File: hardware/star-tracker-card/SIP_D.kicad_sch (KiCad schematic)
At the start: 22 parts, among them J3 CONN_03LONGPADS, U7 OSD3358-512M-BSM

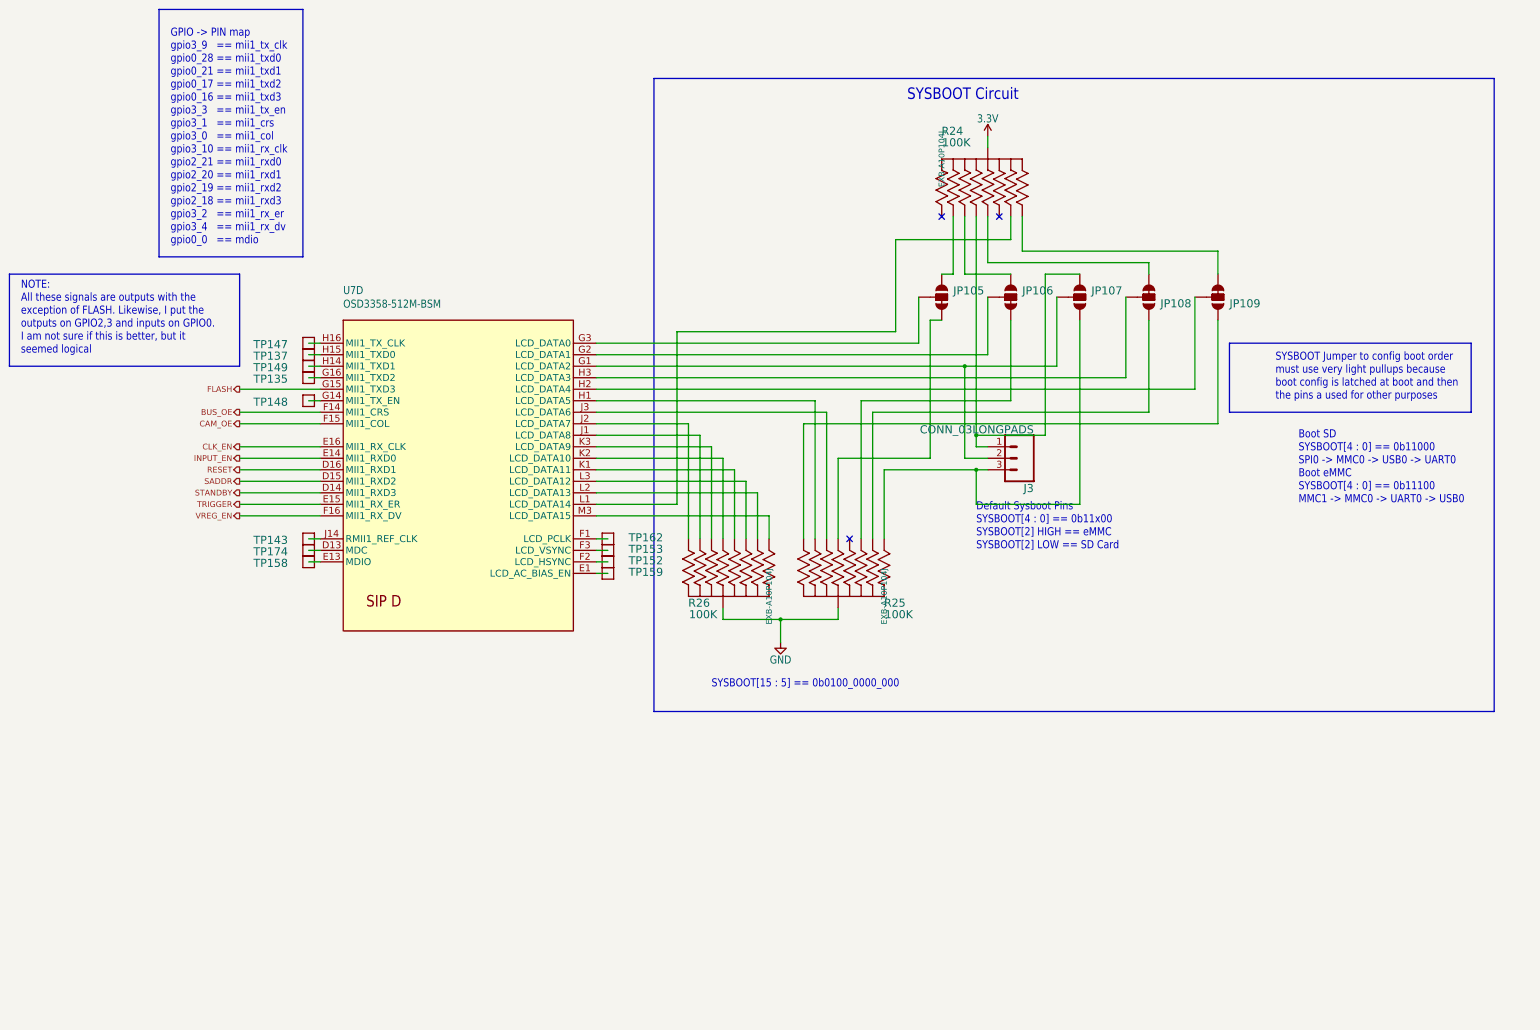
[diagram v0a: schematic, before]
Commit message: Updated Octavo schematic
Removed many testpoints, added filter to 1.8v reference, tied some signals to ground with pull down resistor, added NCs to multiple pins.
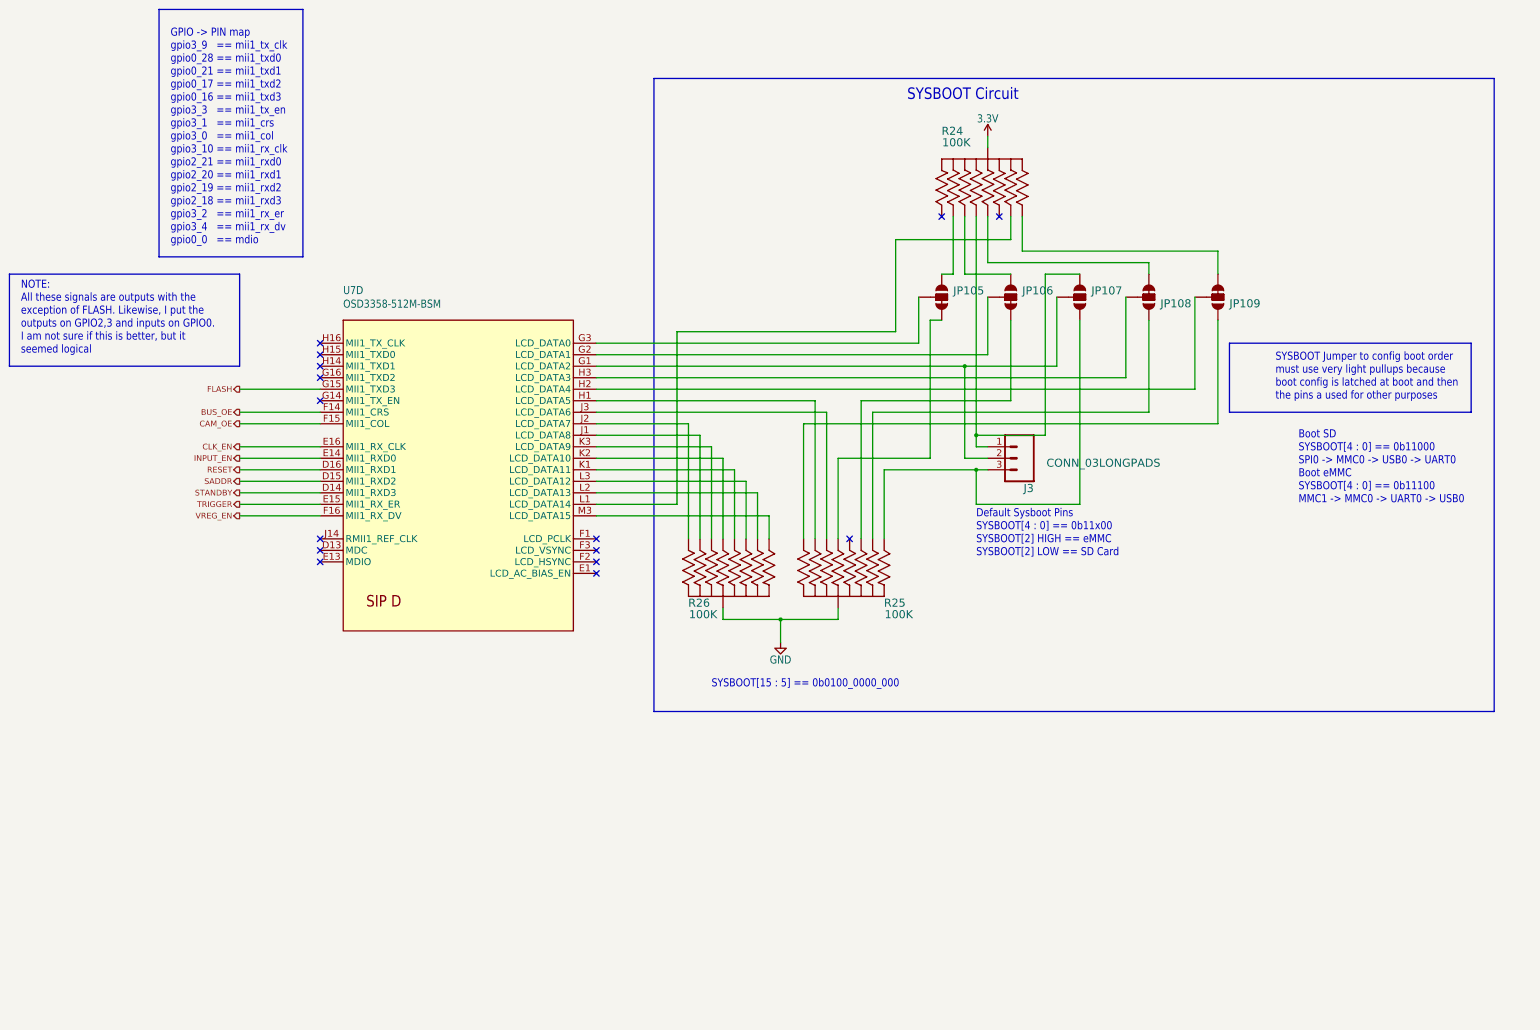
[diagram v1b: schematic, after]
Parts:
- removed TP135, TP137, TP143, TP147, TP148, TP149, TP152, TP153, TP158, TP159, TP162, TP174: TEST-POINT3X4, oresat-misc:TestPoint_Pad_D1.0mm, symbol oresat-misc:Test-Point-1mm-round
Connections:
- no-connect marks 3 -> 15

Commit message: Update
Update to the octavo schematic
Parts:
- removed J3: CONN_03LONGPADS, star-tracker-card:1X03_LONGPADS, symbol star-tracker-card-eagle-import:CONN_03LONGPADS
- removed JP105, JP106, JP108, JP109: JUMPER-SMT_3_1-NC_TRACE_SILK, star-tracker-card:SMT-JUMPER_3_1-NC_TRACE_SILK, symbol star-tracker-card-eagle-import:JUMPER-SMT_3_1-NC_TRACE_SILK
- removed JP107: JUMPER-SMT_3_NO_SILK, star-tracker-card:SMT-JUMPER_3_NO_SILK, symbol star-tracker-card-eagle-import:JUMPER-SMT_3_NO_SILK
- added J6: Conn_01x02, Connector_PinHeader_2.54mm:PinHeader_1x02_P2.54mm_Vertical, symbol Connector_Generic:Conn_01x02
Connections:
- net GND: now also J6.2 (Pin_2)
- net at R25.1 (11): now also U7.G3 (LCD_DATA0)
- net at R25.2 (22): now also U7.G2 (LCD_DATA1)
- net at R24.8 (88): now also U7.G1 (LCD_DATA2), J6.1 (Pin_1)
- net at U7.H2 (LCD_DATA4): now also R24.6 (66)
- net at U7.H3 (LCD_DATA3): now also R24.3 (33)
- no-connect marks 15 -> 20
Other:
- note added: "0"
- note added: "1"
- note added: "SYSBOOT[2] HIGH = eMMC SYSBOOT[2] LOW = uSD"
- moved on the sheet: R25, R26

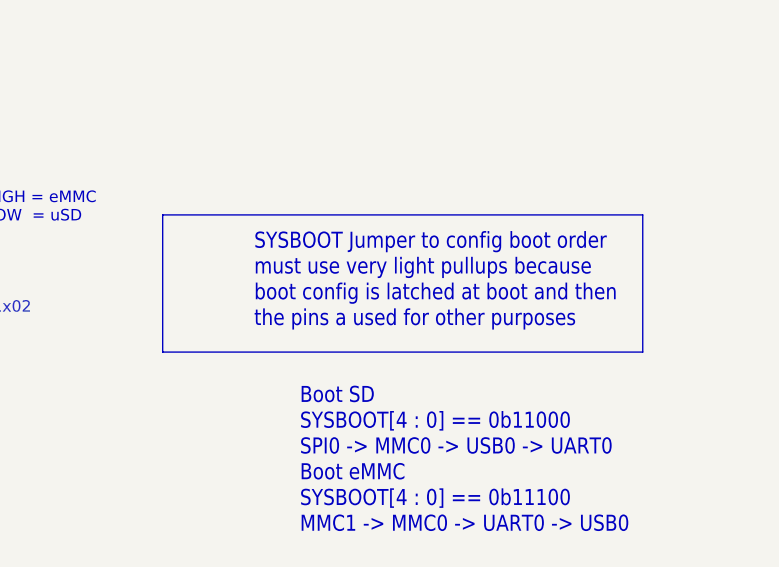
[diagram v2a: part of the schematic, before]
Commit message: Small Update
Removed couple more test points added 2 100nF caps and added text to out put possible pins connected to pull down resistors.
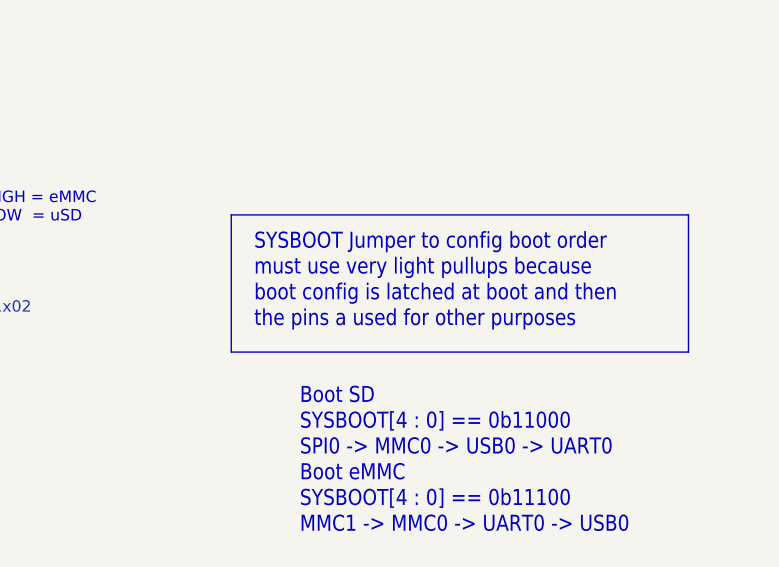
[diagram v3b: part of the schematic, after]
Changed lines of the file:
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@@
 	(polyline
 		(pts
-			(xy 327.66 132.08) (xy 381 132.08)
+			(xy 335.28 132.08) (xy 386.08 132.08)
 		)
 		(stroke
@@
 	(polyline
 		(pts
-			(xy 327.66 116.84) (xy 327.66 132.08)
+			(xy 335.28 116.84) (xy 335.28 132.08)
 		)
 		(stroke
@@
 	(polyline
 		(pts
-			(xy 381 116.84) (xy 327.66 116.84)
+			(xy 386.08 116.84) (xy 335.28 116.84)
 		)
 		(stroke
@@
 	(polyline
 		(pts
-			(xy 381 132.08) (xy 381 116.84)
-		)
-		(stroke
+			(xy 386.08 132.08) (xy 386.08 116.84)
+		)
+		(stroke

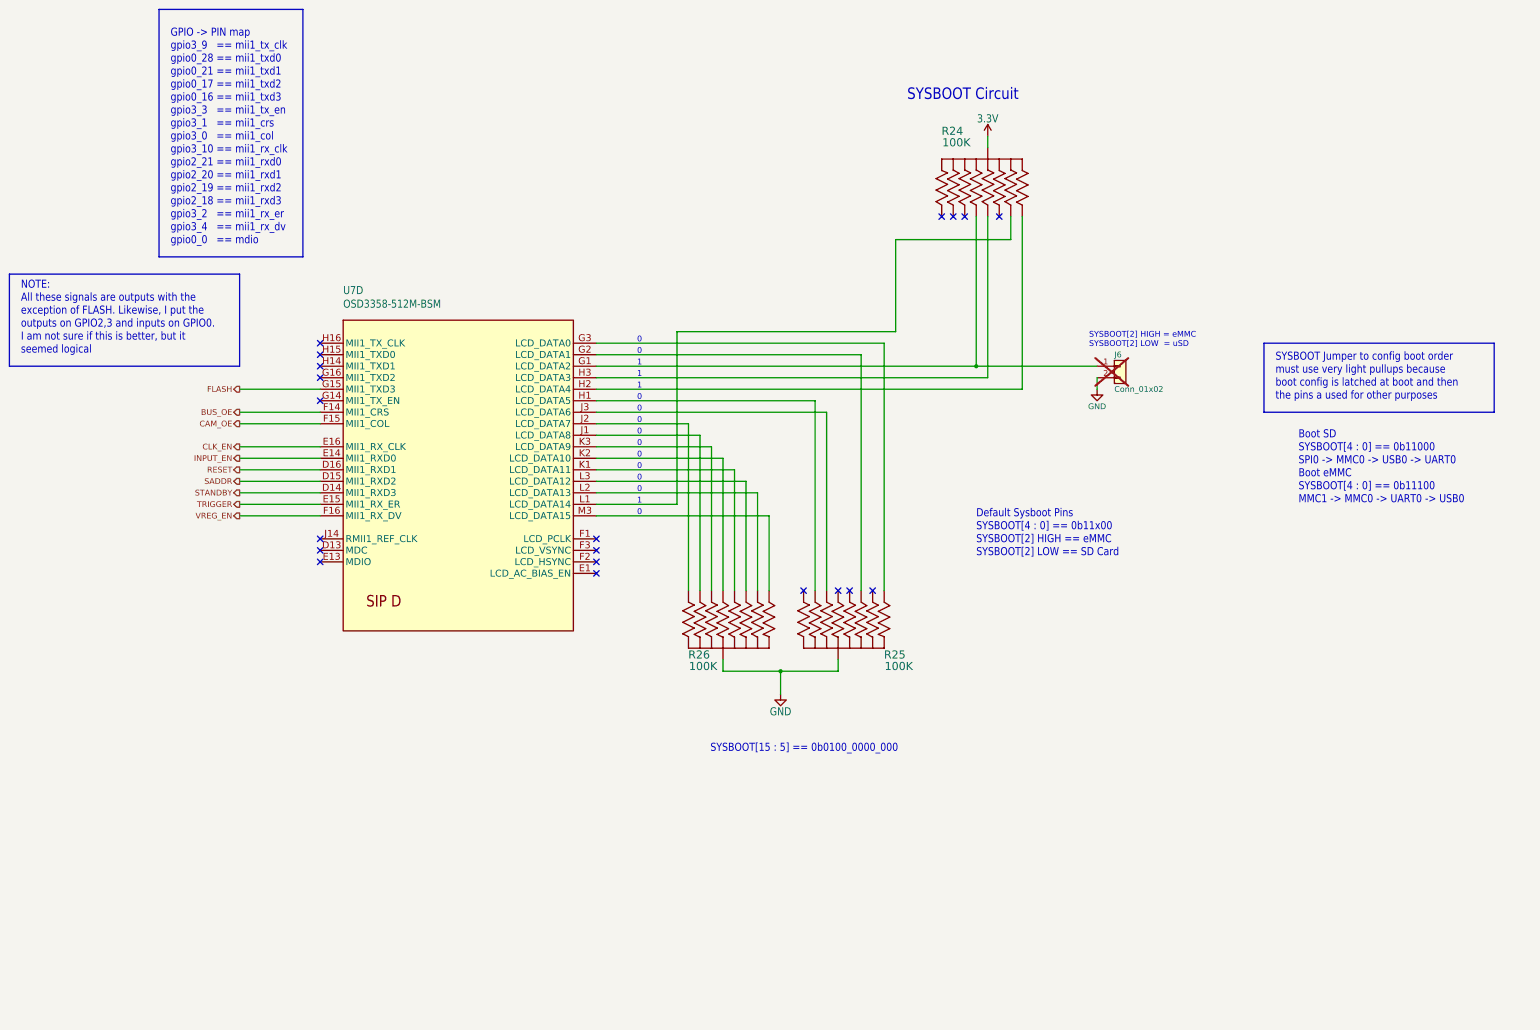
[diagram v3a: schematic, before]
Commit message: Big almost-done cleanup
Fixed a bunch of things in the schematic. Compared against C3 Octavo. Fixed all weird ERCs. Cleaned up a lot of planes on the layout. Moved uart switch, rerouted a bunch of traces for better layout. Fixed library issues, and board/sch sync issues.
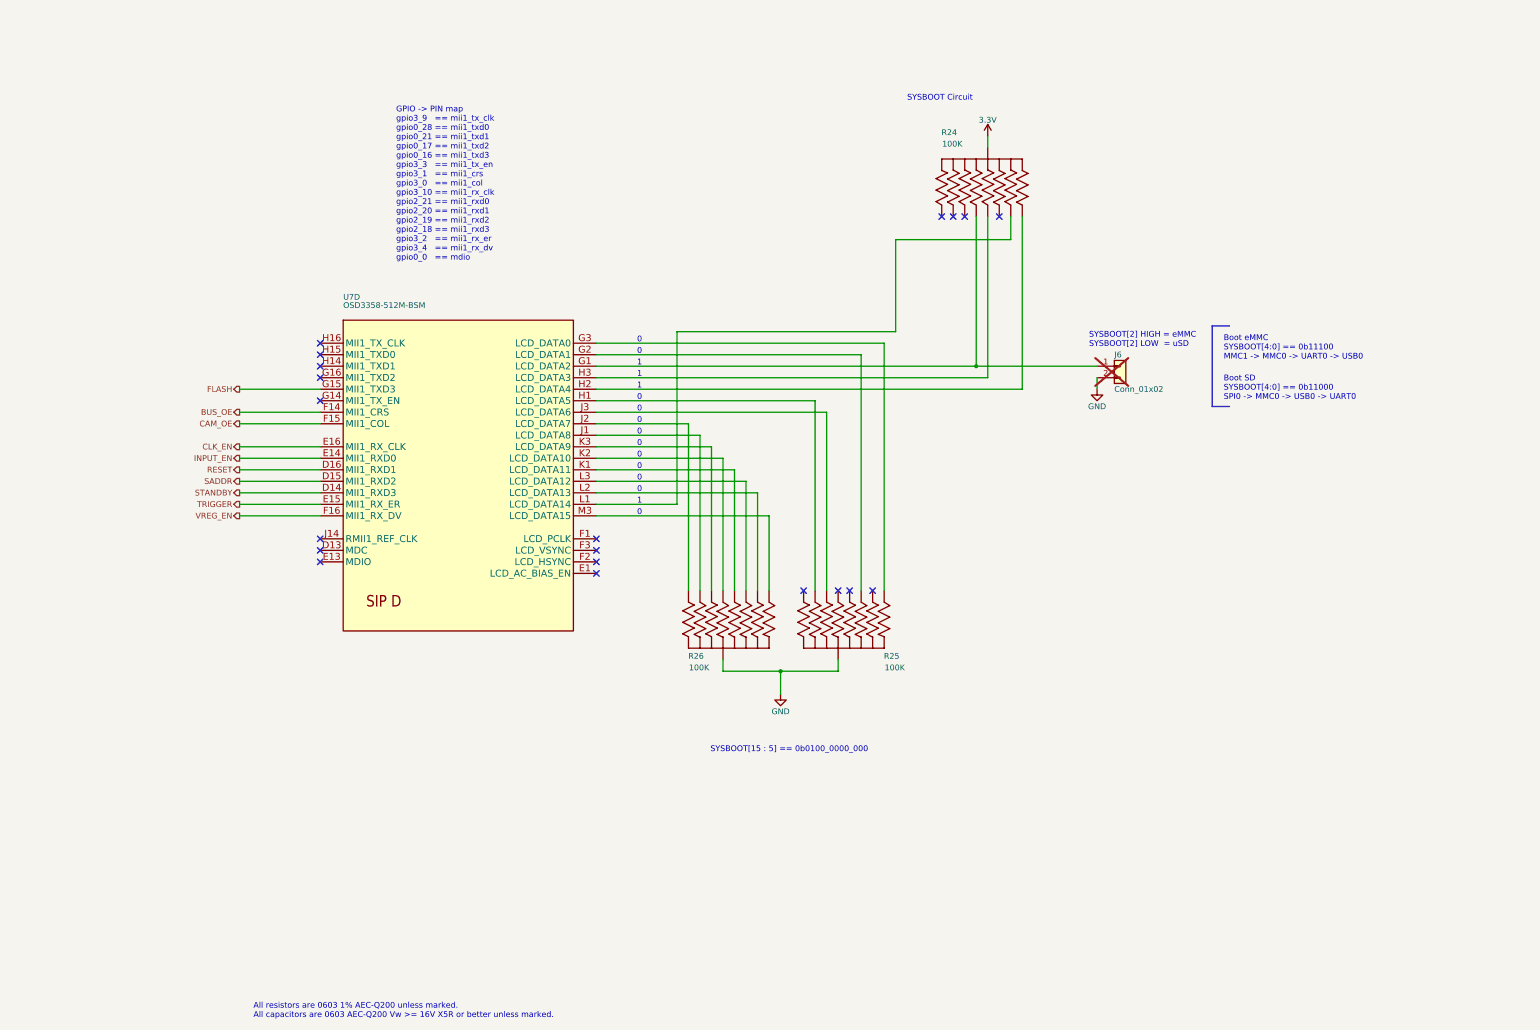
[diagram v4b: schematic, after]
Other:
- note added: "All resistors are 0603 1% AEC-Q200 unless marked. All capacitors are 0603 AEC-Q200 Vw >= 16V X5R or better unless marked."
- note added: "Boot SD SYSBOOT[4:0] == 0b11000 SPI0 -> MMC0 -> USB0 -> UART0"
- note added: "Boot eMMC SYSBOOT[4:0] == 0b11100 MMC1 -> MMC0 -> UART0 -> USB0"
- note removed: "Boot SD SYSBOOT[4 : 0] == 0b11000 SPI0 -> MMC0 -> USB0 -> UART0 Boot eMMC SYSBOOT[4 : 0] == 0b11100 MMC1 -> MMC0 -> UART0 -> USB0"
- note removed: "Default Sysboot Pins SYSBOOT[4 : 0] == 0b11x00 SYSBOOT[2] HIGH == eMMC SYSBOOT[2] LOW == SD Card"
- note removed: "NOTE: All these signals are outputs with the exception of FLASH. Likewise, I put the outputs on GPIO2,3 and inputs on GPIO0. I am not sure if this is better, but it seemed logical"
- note removed: "SYSBOOT Jumper to config boot order must use very light pullups because boot config is latched at boot and then the pins a used for other purposes"
- company: (none) -> Portland State Aerospace Society
- title: (none) -> OreSat Star Tracker

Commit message: BOM 99% completed, push for final review
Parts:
- R24, R25, R26: DIS (none) -> DigiKey; MFR (none) -> Panasonic Industry
- U7: DIS (none) -> DigiKey; DPN (none) -> 1676-OSD3358-1G-ISM-ND; MFR (none) -> Octavo Systems LLC; MPN (none) -> OSD3358-1G-ISM
